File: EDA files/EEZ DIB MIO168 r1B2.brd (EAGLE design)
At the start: 146 x 95 mm, 296 parts, among them IC1 M24C32-WMN6P, IC10 DAC7760IPWPR, IC11 DAC7760IPWPR, IC12 OPA376AIDBVR, IC13 DAC7563TDGSR, IC14 OPA2196IDR, IC15 BTS3408G, IC16 BTS3408G, IC17 BTS3408G, IC18 BTS3408G, IC19 74HC126PW,118, IC2 Si8641BB-B-IS1, IC20 TL431B, IC21 DG468DV-T1-E3, IC22 DG468DV-T1-E3, IC23 DG468DV-T1-E3, IC24 DG468DV-T1-E3, IC25 DG468DV-T1-E3, IC26 DG468DV-T1-E3, IC27 DG468DV-T1-E3, IC28 DG468DV-T1-E3, IC29 DG468DV-T1-E3, IC3 Si8641BB-B-IS1, IC30 DG468DV-T1-E3, IC31 DG468DV-T1-E3, IC32 DG468DV-T1-E3, IC33 DG468DV-T1-E3, IC34 DG468DV-T1-E3, IC35 OPA376AIDBVR, IC36 ADS8674IDBT, IC4 L78L12, IC5 LP2985-50DBVR, IC6 LP2985-33DBVR, IC7 L79L12, IC8 STM32F446ZCT6, IC9 OPA2196IDR, J1 4907, J2 503398-1892, Q1 2N7002PS,115, Q10 BSS169, Q11 BSS169, Q12 BSS169, Q13 BSS169, Q2 2N7002PS,115, Q3 2N7002PS,115, Q4 2N7002PS,115, Q5 2N7002PS,115, Q6 BSS169, Q7 BSS169, Q8 BSS169, Q9 BSS169, X1 77317-104-28LF, X2 SSW-106-02-S-S, X3 691327310016, X4 691327310016, Y1 25MHz

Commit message: #1 fixed
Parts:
- moved C67 3.55 mm to (48.7, 29.7), turned to 0 degrees
- moved IC12 0.19 mm to (48.6, 32.3)
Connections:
- net GND: now also IC12.2; no longer IC12.5
- net N$71: now also IC12.5; no longer IC12.2
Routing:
- net N$71: track 21.5 -> 27.0 mm
- net -12V_ISO: track 263.3 -> 263.9 mm
- added copper zone on layer 16, net GND
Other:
- board text added: "EEZ DIB MIO168 (04/2020 r1B2)"
- board text added: "EEZ DIB MIO168 (04/2020 r1B2) Project source code: github.com/eez-open"
- board text removed: "EEZ DIB MIO168 (03/2020 r1B1)"
- board text removed: "EEZ DIB MIO168 (03/2020 r1B1) Project source code: github.com/eez-open"

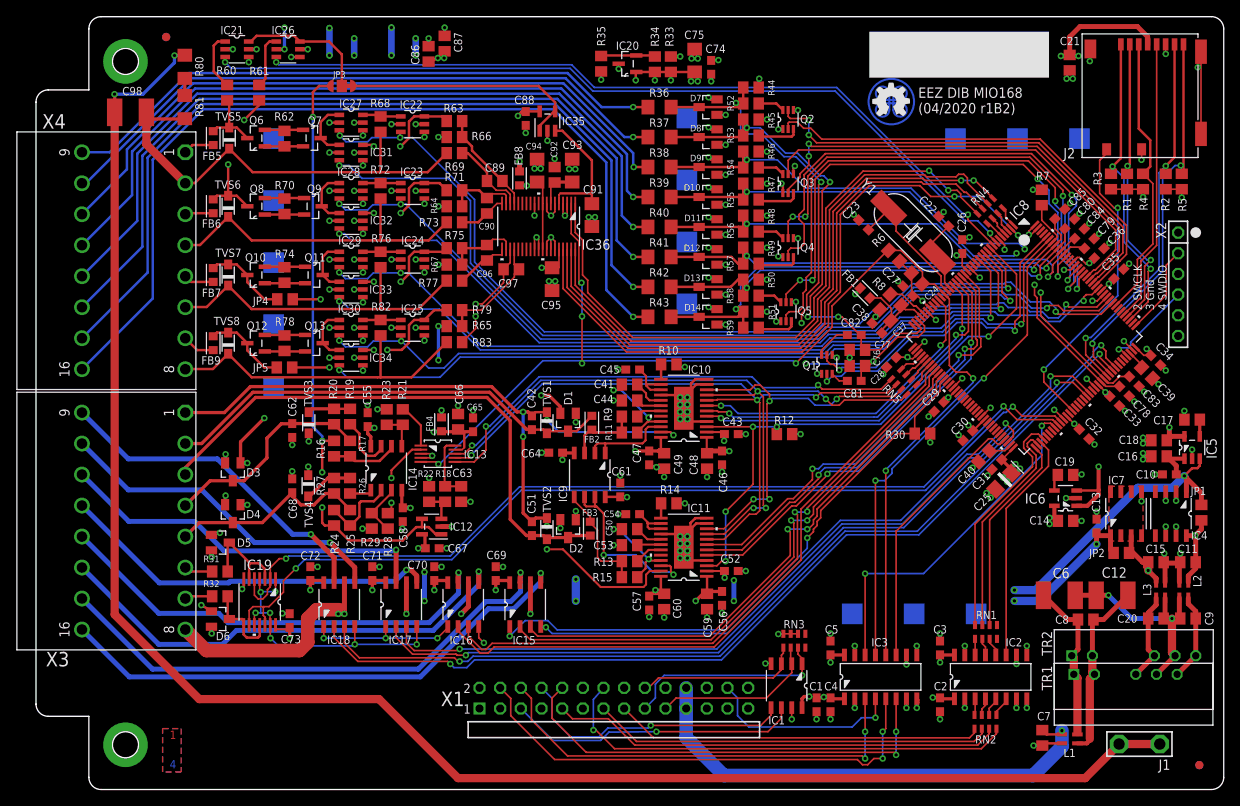
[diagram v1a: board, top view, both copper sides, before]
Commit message: Slave SPI moved to SPI4
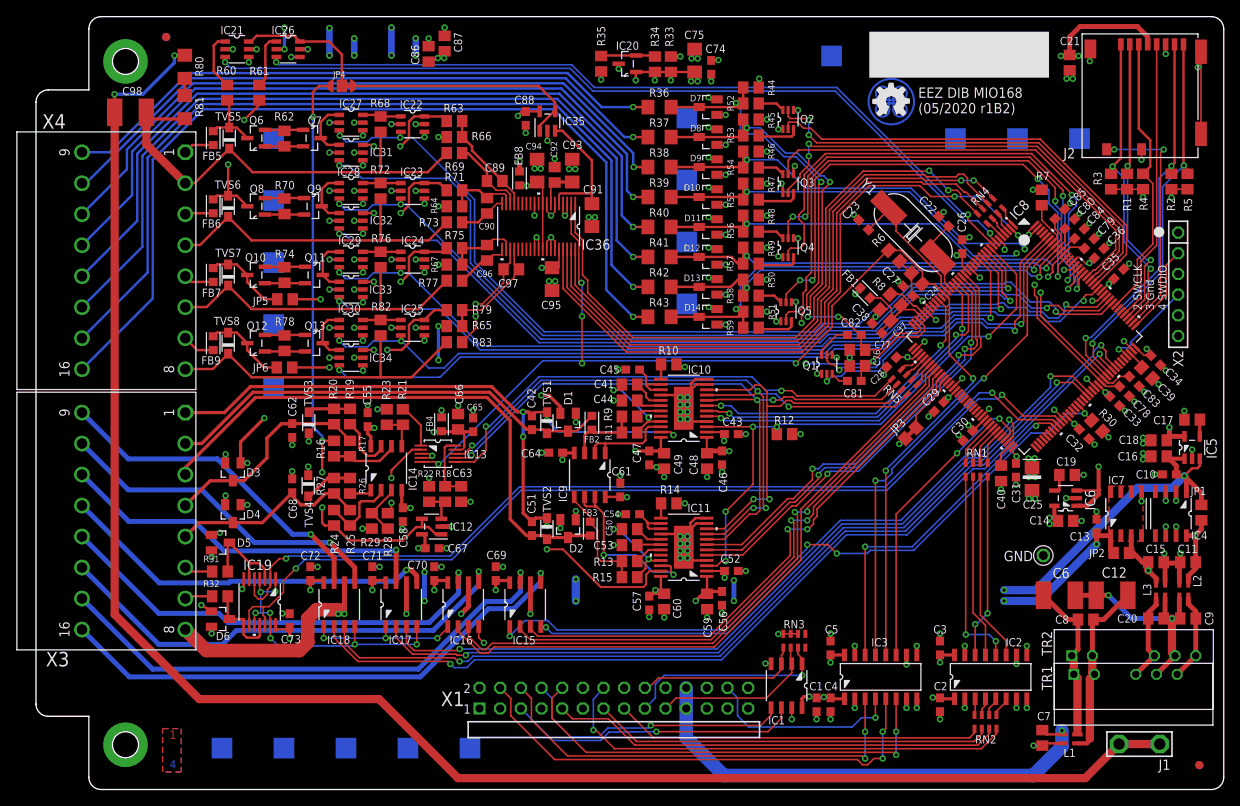
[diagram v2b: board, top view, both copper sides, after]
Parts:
- added GND: (no value), EEZ_Lib1:PCB_SHIELD_TAB
- added JP6: JP2-CUT-0805, EEZ_Lib1:R_0805
- JP3: value JP3-CUT -> JP2-NOCUT-0805; device EEZ_Lib1:JP3-CUT -> EEZ_Lib1:JP2-0805-NOCUT
- JP4: value JP2-CUT-0805 -> JP3-CUT; device EEZ_Lib1:R_0805 -> EEZ_Lib1:JP3-CUT
- moved JP3 81.9 mm to (107.5, 43.8), turned to 45 degrees
- moved JP4 27.1 mm to (37.6, 86.5), turned to 180 degrees
- moved R30 21.5 mm to (130.4, 44.7), turned to 135 degrees
- moved RN1 20.0 mm to (115.6, 39.3)
- moved JP5 8.38 mm to (30.6, 60.3)
- moved C25 3.50 mm to (122.4, 38.2), turned to 270 degrees
- moved C40 2.96 mm to (118.6, 38.9), turned to 90 degrees
- moved C31 2.45 mm to (120.5, 39.2), turned to 270 degrees
- moved SH1 2.22 mm to (122.4, 39.2), turned to 0 degrees
- moved R5 0.70 mm to (141.5, 74.7)
- moved R2 0.70 mm to (139.6, 74.7)
- moved C19 0.19 mm to (126.7, 38.7)
- moved RN5 0.06 mm to (106.7, 50.1)
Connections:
- new net N$11: IC8.48, JP3.2
- new net N$72: IC2.11, RN1.3
- net !OUT_FAULT: now also IC8.88; no longer IC8.48
- net 1V25_REF: now also JP4.NO; no longer JP3.NO
- net GND: now also GND.1, JP3.1
- net MISO: now also IC8.66, RN1.6; no longer IC2.11, IC8.75
- net MOSI: now also IC8.67, RN1.5; no longer IC8.76, RN1.8
- net N$118: now also RN1.1; no longer RN1.3
- net N$12: now also RN1.4; no longer RN1.1
- net N$136: now also JP5.1; no longer JP4.1
- net N$137: now also JP6.1; no longer JP5.1
- net N$20: now also JP4.COM; no longer JP3.COM
- net N$28: now also JP6.2; no longer JP5.2
- net N$31: now also JP4.NC; no longer JP3.NC
- net N$87: now also JP5.2; no longer JP4.2
- net NSS: now also IC8.64, RN1.8; no longer IC8.73, RN1.6
- net SCLK: now also IC8.65; no longer IC8.74
- net SD_DETECT: now also IC8.110; no longer IC8.86
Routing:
- net MOSI: track 29.0 -> 4.18 mm
- net MISO: track 28.7 -> 4.76 mm
- net N$72: track 0.00 -> 23.2 mm
- net N$118: track 2.30 -> 25.1 mm, vias 0 -> 2
- net SCLK: track 27.3 -> 5.34 mm
- net N$12: track 1.99 -> 22.7 mm, vias 0 -> 2
- net N$116: track 2.14 -> 22.6 mm
- net NSS: track 24.8 -> 5.92 mm
- net !OUT_FAULT: track 100.1 -> 115.7 mm, vias 5 -> 7
- net SD_DETECT: track 38.9 -> 30.5 mm
- net N$11: track 0.00 -> 7.43 mm
- net IRQ: track 33.8 -> 38.2 mm, vias 0 -> 2
- net +3V3_MCU: track 44.1 -> 42.3 mm, vias 15 -> 16
- net PWM#1: track 113.5 -> 114.8 mm
- net PWM#2: track 115.9 -> 117.1 mm
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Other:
- board text added: "EEZ DIB MIO168 (05/2020 r1B2)"
- board text added: "EEZ DIB MIO168 (05/2020 r1B2) Project source code: github.com/eez-open"
- board text removed: "EEZ DIB MIO168 (04/2020 r1B2)"
- board text removed: "EEZ DIB MIO168 (04/2020 r1B2) Project source code: github.com/eez-open"

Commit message: #2
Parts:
- moved C41 0.57 mm to (72.4, 49.8)
- moved C44 0.57 mm to (72.4, 47.8)
- moved C50 0.57 mm to (72.4, 32.0)
- moved C53 0.57 mm to (72.4, 30.0)
- moved C52 0.38 mm to (85.5, 26.5)
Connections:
- net N$27 renamed +VSENSE2
- net N$63 renamed +VSENSE1
- net N$64 renamed -VSENSE2
- net N$79 renamed -VSENSE1
- net -12V_ISO: now also IC10.25, IC11.25
- net GND: no longer IC10.25, IC11.25
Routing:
- net -12V_ISO: track 263.9 -> 248.1 mm, vias 22 -> 38
- net PWM#1: track 114.8 -> 124.7 mm, vias 2 -> 4
- net PWM#2: track 117.1 -> 125.3 mm, vias 2 -> 4
- net GND: track 284.0 -> 276.0 mm, vias 187 -> 177
- net N$1: track 63.8 -> 69.2 mm, vias 5 -> 0
- net +3V3_ISO: track 52.2 -> 53.3 mm
- net HART#1: track 3.16 -> 3.83 mm
- net !DAC_ALARM: track 74.2 -> 74.9 mm
- net N$19: track 3.41 -> 3.99 mm
- net HART#2: track 2.93 -> 3.50 mm
- net +12V_ISO: track 260.0 -> 260.5 mm
- added copper zone on layer 15, net -12V_ISO
- added copper zone on layer 16, net -12V_ISO
- removed copper zone on layer 16, net GND
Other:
- board text added: "EEZ DIB MIO168 (06/2020 r1B2)"
- board text added: "EEZ DIB MIO168 (06/2020 r1B2) Project source code: github.com/eez-open"
- board text removed: "EEZ DIB MIO168 (05/2020 r1B2)"
- board text removed: "EEZ DIB MIO168 (05/2020 r1B2) Project source code: github.com/eez-open"

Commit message: #3
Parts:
- removed JP6: JP2-CUT-0805, EEZ_Lib1:R_0805
- C21: value 4u7 -> N.C.
- J2: value 503398-1892 -> N.C.
- JP3: value JP2-NOCUT-0805 -> JP3-CUT; device EEZ_Lib1:JP2-0805-NOCUT -> EEZ_Lib1:JP3-CUT
- JP4: value JP3-CUT -> JP2-CUT-0805; device EEZ_Lib1:JP3-CUT -> EEZ_Lib1:R_0805
- R1, R2, R3, R4, R5: value 47K -> N.C.
- moved JP3 81.9 mm to (37.6, 86.5), turned to 180 degrees
- moved JP4 27.1 mm to (30.6, 60.3), turned to 0 degrees
- moved RN4 23.5 mm to (106.7, 50.1), turned to 315 degrees
- moved RN5 22.0 mm to (125.9, 39.3), turned to 0 degrees
- moved JP5 8.38 mm to (30.5, 51.9)
- moved C19 7.91 mm to (125.5, 30.9), turned to 90 degrees
- moved C14 7.01 mm to (119.8, 31.1), turned to 270 degrees
- moved R12 6.38 mm to (86.6, 40.4), turned to 90 degrees
- moved IC6 6.18 mm to (122.6, 31.1), turned to 90 degrees
- moved GND 5.38 mm to (118.7, 27.2)
- moved R11 0.57 mm to (72.4, 43.9)
- moved R13 0.57 mm to (72.4, 28.1)
- moved R15 0.57 mm to (72.4, 26.1)
- moved R9 0.57 mm to (72.4, 45.8)
- moved FB2 0.13 mm to (68.2, 45.1)
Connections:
- removed net N$11: IC8.48, JP3.2
- removed net N$39: IC8.1, RN4.8
- removed net N$40: IC8.3, RN4.7
- removed net N$41: IC8.4, RN4.6
- removed net N$44: IC8.5, RN4.5
- new net N$27: IC8.75, RN5.6
- new net N$29: IC8.76, RN5.5
- new net N$34: IC8.73, RN5.8
- new net N$37: IC8.74, RN5.7
- net !ADC_CS: now also RN5.1; no longer RN4.2
- net !DAC_CS_DUAL: now also RN4.1; no longer RN5.1
- net 1V25_REF: now also JP3.NO; no longer JP4.NO
- net ADC_IRQ: now also IC8.77; no longer IC8.2
- net ADC_MISO: now also RN5.3; no longer RN4.3
- net ADC_MOSI: now also RN5.4; no longer RN4.4
- net ADC_SCLK: now also RN5.2; no longer RN4.1
- net DAC_MISO: now also RN4.3; no longer RN5.3
- net DAC_MOSI: now also RN4.4; no longer RN5.4
- net DAC_SCLK: now also RN4.2; no longer RN5.2
- net GND: now also IC8.48; no longer JP3.1
- net N$100: now also RN4.6; no longer RN5.6
- net N$103: now also RN4.5; no longer RN5.5
- net N$136: now also JP4.1; no longer JP5.1
- net N$137: now also JP5.1; no longer JP6.1
- net N$20: now also JP3.COM; no longer JP4.COM
- net N$28: now also JP5.2; no longer JP6.2
- net N$31: now also JP3.NC; no longer JP4.NC
- net N$81: now also RN4.8; no longer RN5.8
- net N$87: now also JP4.2; no longer JP5.2
- net N$98: now also RN4.7; no longer RN5.7
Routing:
- net +5V_ISO: track 271.9 -> 283.7 mm, vias 5 -> 4
- net N$11: track 7.43 -> 0.00 mm
- net ADC_MOSI: track 79.9 -> 86.4 mm
- net ADC_IRQ: track 83.4 -> 89.9 mm, vias 2 -> 0
- net N$29: track 0.00 -> 4.89 mm
- net +VSENSE2: track 22.4 -> 17.8 mm
- net N$27: track 0.00 -> 4.17 mm
- net ADC_MISO: track 75.8 -> 79.3 mm
- net N$37: track 0.00 -> 3.44 mm
- net -VSENSE1: track 22.3 -> 19.1 mm
- net DAC_MISO: track 48.3 -> 45.5 mm, vias 2 -> 3
- net N$40: track 2.67 -> 0.00 mm
- net N$39: track 2.63 -> 0.00 mm
- net N$34: track 0.00 -> 2.54 mm
- net N$41: track 2.50 -> 0.00 mm
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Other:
- board text added: "EEZ DIB MIO168 (07/2020 r1B2)"
- board text added: "EEZ DIB MIO168 (07/2020 r1B2) Project source code: github.com/eez-open"
- board text removed: "EEZ DIB MIO168 (06/2020 r1B2)"
- board text removed: "EEZ DIB MIO168 (06/2020 r1B2) Project source code: github.com/eez-open"

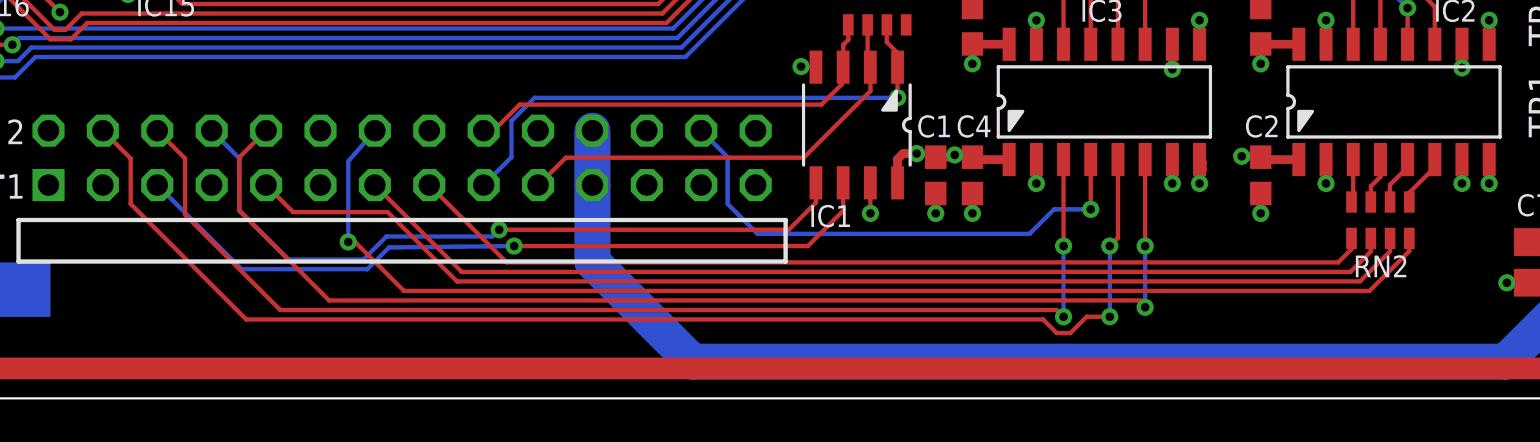
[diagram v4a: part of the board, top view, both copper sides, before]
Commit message: IRQ selection jumper
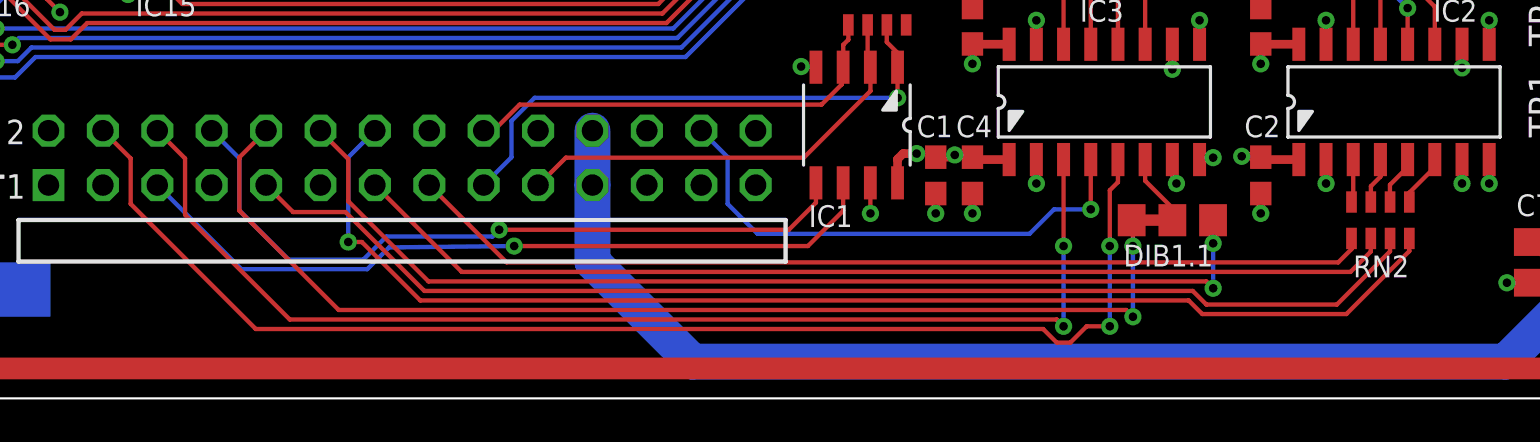
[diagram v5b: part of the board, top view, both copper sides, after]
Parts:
- added DIB1.1: JP3-CUT-0805-ROTATED, EEZ_Lib1:JP3-0805-CUT2
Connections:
- new net DIB_CSB: DIB1.1.NO, X1.12
- new net N$11: DIB1.1.COM, IC3.6
- net DIB_IRQ: now also DIB1.1.NC; no longer IC3.6
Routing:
- net DIB_CSB: track 0.00 -> 49.1 mm, vias 0 -> 2
- net N$11: track 0.00 -> 3.36 mm
- net DIB_IRQ: track 55.5 -> 52.6 mm
- net N$101: track 57.5 -> 58.5 mm
- net N$69: track 55.5 -> 56.4 mm
- net DIB_NRESET: track 60.0 -> 60.6 mm
- net OE_SYNC: track 54.8 -> 55.4 mm
- net GNDIO: track 13.1 -> 12.6 mm
